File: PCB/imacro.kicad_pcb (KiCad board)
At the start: 2 copper layers, 57.2 x 83.3 mm, 29 parts, among them SW0:0 Choc, SW0:1 Choc, SW0:2 Choc, SW1 TOGGLE, SW1:0 Choc, SW1:1 Choc, SW1:2 Choc, SW2:0 Choc, SW2:1 Choc, SW2:2 Choc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

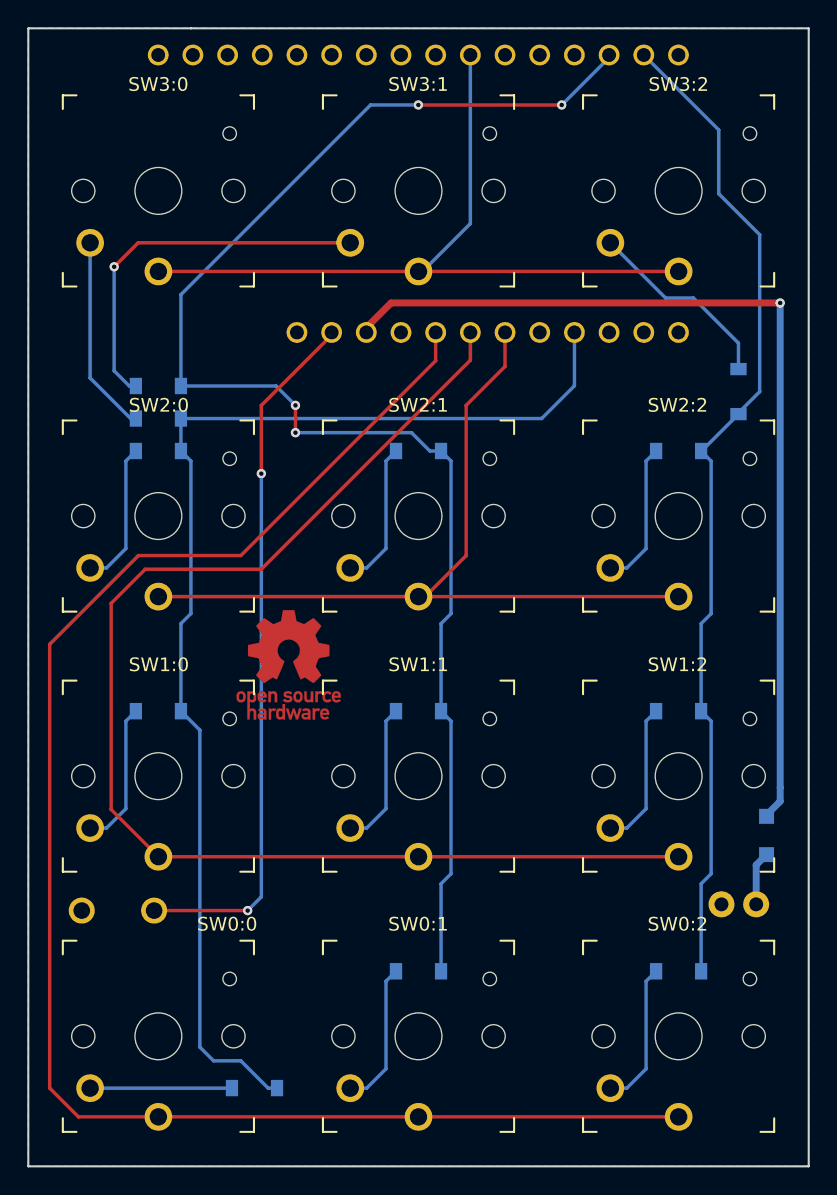
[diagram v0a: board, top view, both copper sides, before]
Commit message: Clean up some traces; avoid vias in power trace; avoid vias under components
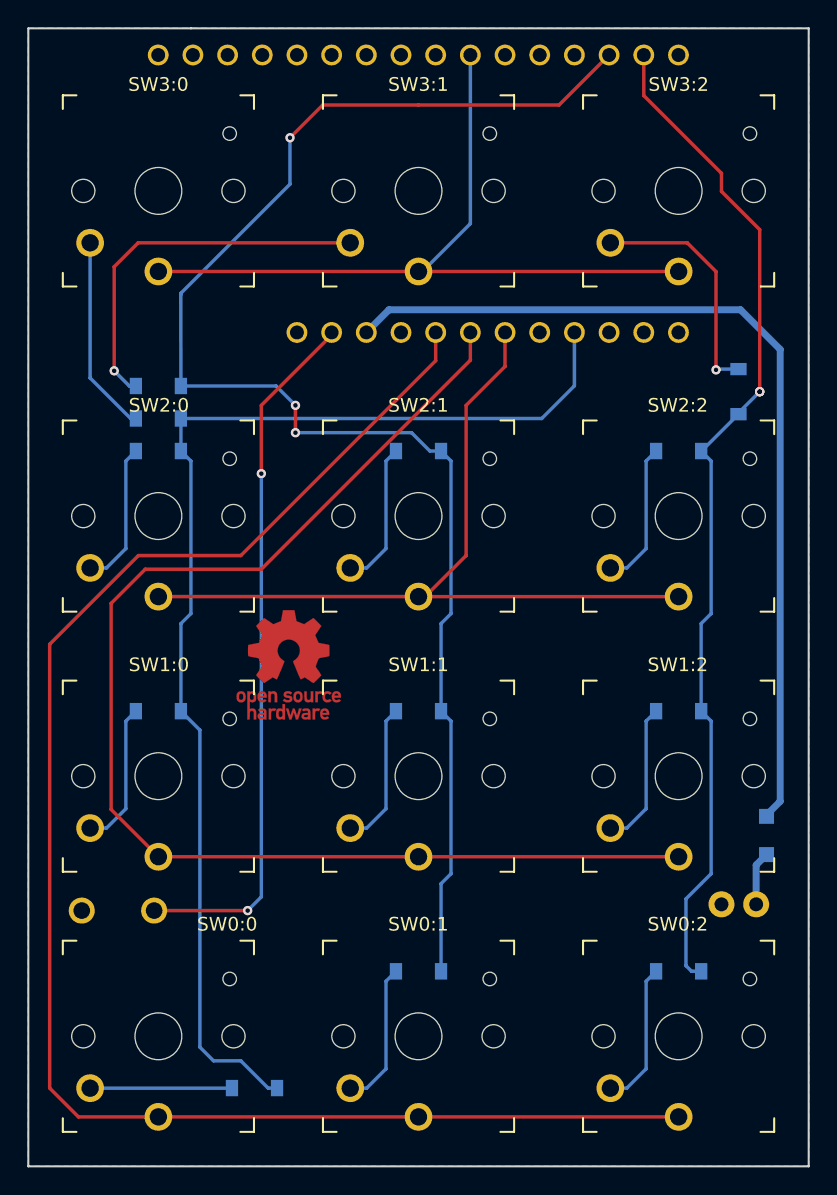
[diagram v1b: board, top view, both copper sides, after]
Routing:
- net Net-(D3:2-Pad2): track 14.3 -> 17.5 mm, vias 0 -> 1
- net /5V_USB: track 70.0 -> 66.9 mm, vias 1 -> 0
- net /COL1: track 106.9 -> 109.2 mm, vias 4 -> 3
- net /COL2: track 73.6 -> 75.0 mm, vias 0 -> 2
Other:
- board text added: "v1.1"
- board text removed: "v1.0"
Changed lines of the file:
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@@
     (thickness 1.6)
     (drawings 10)
-    (tracks 155)
+    (tracks 162)
     (zones 0)
     (modules 29)
@@
     (effects (font (size 0.738 0.738) (thickness 0.1845)) (justify mirror))
   )
-  (gr_text v1.0 (at 125.5 134.5) (layer B.SilkS)
+  (gr_text v1.1 (at 125.5 134.5) (layer B.SilkS)
     (effects (font (size 1.5 1.5) (thickness 0.3)) (justify mirror))
   )
@@
   (segment (start 86.34375 130.00625) (end 86.35 130) (width 0.254) (layer B.Cu) (net 2))
   (segment (start 86.65 130) (end 86.65 129.65) (width 0.254) (layer B.Cu) (net 2))
-  (segment (start 82.6125 78.58125) (end 82.6125 71.8875) (width 0.254) (layer B.Cu) (net 3))
-  (segment (start 110.5 58) (end 113.97 54.53) (width 0.254) (layer B.Cu) (net 3))
-  (via (at 110.5 58) (size 0.6858) (drill 0.3302) (layers F.Cu B.Cu) (net 3))
-  (segment (start 100 58) (end 110.5 58) (width 0.254) (layer F.Cu) (net 3))
-  (via (at 100 58) (size 0.6858) (drill 0.3302) (layers F.Cu B.Cu) (net 3))
-  (segment (start 96.5 58) (end 100 58) (width 0.254) (layer B.Cu) (net 3))
-  (segment (start 82.6125 71.8875) (end 96.5 58) (width 0.254) (layer B.Cu) (net 3))
   (segment (start 113.97 54.53) (end 113.97 54.34) (width 0.254) (layer B.Cu) (net 3))
   (segment (start 101.6625 83.34375) (end 100.84375 83.34375) (width 0.254) (layer B.Cu) (net 3))
@@
   (segment (start 102.39375 114.3) (end 102.39375 103.125) (width 0.25) (layer B.Cu) (net 3))
   (segment (start 101.6625 115.03125) (end 102.39375 114.3) (width 0.25) (layer B.Cu) (net 3))
+  (segment (start 110.31 58) (end 100 58) (width 0.254) (layer F.Cu) (net 3))
+  (segment (start 113.97 54.34) (end 110.31 58) (width 0.254) (layer F.Cu) (net 3))
+  (segment (start 93 58) (end 90.6 60.4) (width 0.254) (layer F.Cu) (net 3))
+  (via (at 90.6 60.4) (size 0.6858) (drill 0.3302) (layers F.Cu B.Cu) (net 3))
+  (segment (start 100 58) (end 93 58) (width 0.254) (layer F.Cu) (net 3))
+  (segment (start 90.6 60.4) (end 90.6 63.8) (width 0.254) (layer B.Cu) (net 3))
+  (segment (start 90.6 63.8) (end 82.6 71.8) (width 0.254) (layer B.Cu) (net 3))
+  (segment (start 82.6 71.8) (end 82.6125 71.8875) (width 0.254) (layer B.Cu) (net 3))
+  (segment (start 82.6125 78.58125) (end 82.6 71.8) (width 0.254) (layer B.Cu) (net 3))
   (segment (start 97.63125 122.175) (end 98.3625 121.44375) (width 0.25) (layer B.Cu) (net 4))
   (segment (start 97.63125 128.5875) (end 97.63125 122.175) (width 0.25) (layer B.Cu) (net 4))
@@
   (segment (start 123.444 80.644) (end 123.444 80.556) (width 0.254) (layer B.Cu) (net 5))
   (segment (start 123.444 80.556) (end 125 79) (width 0.254) (layer B.Cu) (net 5))
-  (segment (start 122 59.83) (end 116.51 54.34) (width 0.254) (layer B.Cu) (net 5))
-  (segment (start 122 64.5) (end 122 59.83) (width 0.254) (layer B.Cu) (net 5))
-  (segment (start 125 67.5) (end 122 64.5) (width 0.254) (layer B.Cu) (net 5))
-  (segment (start 125 79) (end 125 67.5) (width 0.254) (layer B.Cu) (net 5))
   (segment (start 120.7125 83.34375) (end 120.74425 83.34375) (width 0.254) (layer B.Cu) (net 5))
   (segment (start 120.74425 83.34375) (end 123.444 80.644) (width 0.254) (layer B.Cu) (net 5))
@@
   (segment (start 121.44375 95.25) (end 121.44375 84.075) (width 0.25) (layer B.Cu) (net 5))
   (segment (start 120.7125 95.98125) (end 121.44375 95.25) (width 0.25) (layer B.Cu) (net 5))
-  (segment (start 120.7125 121.44375) (end 120.7125 115.03125) (width 0.25) (layer B.Cu) (net 5))
   (segment (start 121.44375 103.125) (end 120.7125 102.39375) (width 0.25) (layer B.Cu) (net 5))
   (segment (start 121.44375 114.3) (end 121.44375 103.125) (width 0.25) (layer B.Cu) (net 5))
   (segment (start 120.7125 115.03125) (end 121.44375 114.3) (width 0.25) (layer B.Cu) (net 5))
+  (via (at 125 79) (size 0.6858) (drill 0.3302) (layers F.Cu B.Cu) (net 5))
+  (via (at 125 79) (size 0.6858) (drill 0.3302) (layers F.Cu B.Cu) (net 5))
+  (segment (start 125 67.129908) (end 122.2 64.329908) (width 0.254) (layer F.Cu) (net 5))
+  (segment (start 125 79) (end 125 67.129908) (width 0.254) (layer F.Cu) (net 5))
+  (segment (start 122.2 64.329908) (end 122.2 63) (width 0.254) (layer F.Cu) (net 5))
+  (segment (start 116.51 57.31) (end 116.51 54.34) (width 0.254) (layer F.Cu) (net 5))
+  (segment (start 122.2 63) (end 116.51 57.31) (width 0.254) (layer F.Cu) (net 5))
+  (segment (start 120.0085 121.44375) (end 119.6 121.03525) (width 0.254) (layer B.Cu) (net 5))
+  (segment (start 120.7125 121.44375) (end 120.0085 121.44375) (width 0.254) (layer B.Cu) (net 5))
+  (segment (start 119.6 116.14375) (end 120.7125 115.03125) (width 0.254) (layer B.Cu) (net 5))
+  (segment (start 119.6 121.03525) (end 119.6 116.14375) (width 0.254) (layer B.Cu) (net 5))
   (segment (start 116.68125 122.175) (end 117.4125 121.44375) (width 0.25) (layer B.Cu) (net 6))
   (segment (start 116.68125 128.5875) (end 116.68125 122.175) (width 0.25) (layer B.Cu) (net 6))
   (segment (start 115.2625 130.00625) (end 116.68125 128.5875) (width 0.25) (layer B.Cu) (net 6))
   (segment (start 114.0625 130.00625) (end 115.2625 130.00625) (width 0.25) (layer B.Cu) (net 6))
-  (segment (start 96.19 74.66) (end 96.19 74.31) (width 0.508) (layer F.Cu) (net 7))
-  (segment (start 96.19 74.31) (end 98 72.5) (width 0.508) (layer F.Cu) (net 7))
-  (segment (start 98 72.5) (end 126.5 72.5) (width 0.508) (layer F.Cu) (net 7))
-  (via (at 126.5 72.5) (size 0.6858) (drill 0.3302) (layers F.Cu B.Cu) (net 7))
-  (segment (start 126.5 72.5) (end 126.5 108) (width 0.508) (layer B.Cu) (net 7))
-  (segment (start 126.5 108) (end 126.5 109) (width 0.508) (layer B.Cu) (net 7))
-  (segment (start 126.5 109) (end 125.5 110) (width 0.508) (layer B.Cu) (net 7))
-  (segment (start 125.5 110) (end 125.5 110.1) (width 0.508) (layer B.Cu) (net 7))
   (segment (start 125.5 110.1) (end 125.5 110) (width 0.254) (layer B.Cu) (net 7))
-  (segment (start 96.2025 74.45375) (end 96.2025 74.00375) (width 0.254) (layer F.Cu) (net 7))
+  (segment (start 125.5 110.1) (end 125.5 110) (width 0.508) (layer B.Cu) (net 7))
+  (segment (start 126.5 109) (end 126.5 75.9) (width 0.508) (layer B.Cu) (net 7))
+  (segment (start 125.5 110) (end 126.5 109) (width 0.508) (layer B.Cu) (net 7))
+  (segment (start 126.5 75.9) (end 123.6 73) (width 0.508) (layer B.Cu) (net 7))
+  (segment (start 97.85 73) (end 96.19 74.66) (width 0.508) (layer B.Cu) (net 7))
+  (segment (start 123.6 73) (end 97.85 73) (width 0.508) (layer B.Cu) (net 7))
   (segment (start 124.74 116.54) (end 124.74 113.66) (width 0.508) (layer B.Cu) (net 8))
   (segment (start 124.74 113.66) (end 125.5 112.9) (width 0.508) (layer B.Cu) (net 8))
@@
   (segment (start 79.48025 68.09375) (end 95.0125 68.09375) (width 0.254) (layer F.Cu) (net 16))
   (segment (start 77.724 69.85) (end 79.48025 68.09375) (width 0.254) (layer F.Cu) (net 16))
-  (via (at 77.724 69.85) (size 0.6858) (drill 0.3302) (layers F.Cu B.Cu) (net 16))
-  (segment (start 77.724 77.47) (end 77.724 69.85) (width 0.254) (layer B.Cu) (net 16))
   (segment (start 78.83525 78.58125) (end 77.724 77.47) (width 0.254) (layer B.Cu) (net 16))
-  (segment (start 118.10475 72.136) (end 114.0625 68.09375) (width 0.254) (layer B.Cu) (net 17))
-  (segment (start 120.142 72.136) (end 118.10475 72.136) (width 0.254) (layer B.Cu) (net 17))
-  (segment (start 123.444 75.438) (end 120.142 72.136) (width 0.254) (layer B.Cu) (net 17))
-  (segment (start 123.444 77.344) (end 123.444 75.438) (width 0.254) (layer B.Cu) (net 17))
+  (via (at 77.724 77.47) (size 0.6858) (drill 0.3302) (layers F.Cu B.Cu) (net 16))
+  (segment (start 77.724 69.85) (end 77.724 77.47) (width 0.254) (layer F.Cu) (net 16))
+  (via (at 121.8 77.4) (size 0.6858) (drill 0.3302) (layers F.Cu B.Cu) (net 17))
+  (segment (start 121.856 77.344) (end 121.8 77.4) (width 0.254) (layer B.Cu) (net 17))
+  (segment (start 123.444 77.344) (end 121.856 77.344) (width 0.254) (layer B.Cu) (net 17))
+  (segment (start 119.69375 68.09375) (end 114.0625 68.09375) (width 0.254) (layer F.Cu) (net 17))
+  (segment (start 121.8 70.2) (end 119.69375 68.09375) (width 0.254) (layer F.Cu) (net 17))
+  (segment (start 121.8 77.4) (end 121.8 70.2) (width 0.254) (layer F.Cu) (net 17))
   (segment (start 101.27 74.66) (end 101.27 76.73) (width 0.254) (layer F.Cu) (net 19))
   (segment (start 75.10625 132.10625) (end 80.9625 132.10625) (width 0.254) (layer F.Cu) (net 19))
@@
     (connect_pads (clearance 0.508))
     (min_thickness 0.254)
-    (fill (arc_segments 16) (thermal_gap 0.508) (thermal_bridge_width 0.508))
+    (fill yes (arc_segments 16) (thermal_gap 0.508) (thermal_bridge_width 0.508))
     (polygon
       (pts
@@
     (connect_pads (clearance 0.508))
     (min_thickness 0.254)
-    (fill (arc_segments 16) (thermal_gap 0.508) (thermal_bridge_width 0.508))
+    (fill yes (arc_segments 16) (thermal_gap 0.508) (thermal_bridge_width 0.508))
     (polygon
       (pts
